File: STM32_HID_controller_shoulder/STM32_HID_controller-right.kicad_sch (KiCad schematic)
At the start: 5 parts, among them J4 Conn_01x03_Socket

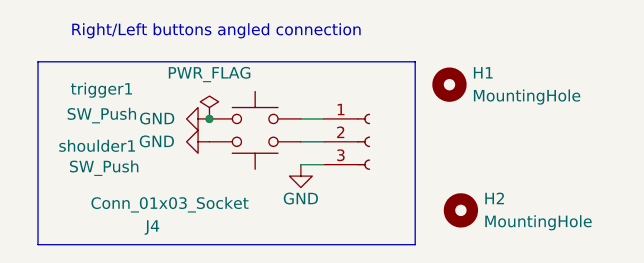
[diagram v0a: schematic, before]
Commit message: changed shoulder to right orientation
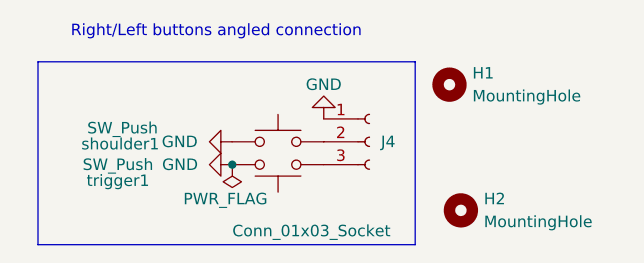
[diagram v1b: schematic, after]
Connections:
- net GND: now also J4.1 (Pin_1); no longer J4.3 (Pin_3)
- net at trigger1.2: now also J4.3 (Pin_3); no longer J4.1 (Pin_1)
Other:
- moved on the sheet: shoulder1, trigger1
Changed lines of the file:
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@@
 	)
 	(junction
-		(at 76.2 62.23)
+		(at 78.74 67.31)
 		(diameter 0)
 		(color 0 0 0 0)
 	)
-	(wire
-		(pts
-			(xy 86.36 62.23) (xy 88.9 62.23)
-		)
-		(stroke
-			(width 0)
-			(type default)
-		)
-	)
-	(wire
-		(pts
-			(xy 86.36 67.31) (xy 88.9 67.31)
-		)
-		(stroke
-			(width 0)
-			(type default)
-		)
-	)
-	(wire
-		(pts
-			(xy 86.36 64.77) (xy 88.9 64.77)
-		)
-		(stroke
-			(width 0)
-			(type default)
-		)
-	)
 	(symbol
 		(lib_id "power:GND")
-		(at 76.2 64.77 270)
+		(at 78.74 64.77 270)
 		(unit 1)
 		(exclude_from_sim no)
@@
 		(dnp no)
 		(property "Reference" "#PWR054"
-			(at 69.85 64.77 0)
+			(at 72.39 64.77 0)
 			(effects
 				(font
@@
 		)
 		(property "Value" "GND"
-			(at 70.358 64.77 90)
+			(at 72.898 64.77 90)
 			(effects
 				(font
@@
 		)
 		(property "Footprint" ""
-			(at 76.2 64.77 0)
+			(at 78.74 64.77 0)
 			(effects
 				(font
@@
 		)
 		(property "Datasheet" ""
-			(at 76.2 64.77 0)
+			(at 78.74 64.77 0)
 			(effects
 				(font
@@
 		)
 		(property "Description" "Power symbol creates a global label with name \"GND\" , ground"
-			(at 76.2 64.77 0)
+			(at 78.74 64.77 0)
 			(effects
 				(font
@@
 	(symbol
 		(lib_id "Switch:SW_Push")
-		(at 81.28 64.77 180)
+		(at 83.82 64.77 0)
+		(mirror y)
 		(unit 1)
 		(exclude_from_sim no)
@@
 		(dnp no)
 		(property "Reference" "shoulder1"
-			(at 63.754 65.278 0)
+			(at 66.294 65.024 0)
 			(effects
 				(font
@@
 		)
 		(property "Value" "SW_Push"
-			(at 64.516 67.564 0)
+			(at 66.548 63.246 0)
 			(effects
 				(font
@@
 		)
 		(property "Footprint" "Button_Switch_THT:SW_PUSH-12mm_Wuerth-430476085716"
-			(at 81.28 69.85 0)
+			(at 83.82 59.69 0)
 			(effects
 				(font
@@
 		)
 		(property "Datasheet" "~"
-			(at 81.28 69.85 0)
+			(at 83.82 59.69 0)
 			(effects
 				(font
@@
 		)
 		(property "Description" "Push button switch, generic, two pins"
-			(at 81.28 64.77 0)
+			(at 83.82 64.77 0)
 			(effects
 				(font
@@
 	(symbol
 		(lib_id "power:GND")
-		(at 86.36 67.31 0)
+		(at 88.9 62.23 180)
 		(unit 1)
 		(exclude_from_sim no)
@@
 		(dnp no)
 		(property "Reference" "#PWR053"
-			(at 86.36 73.66 0)
+			(at 88.9 55.88 0)
 			(effects
 				(font
@@
 		)
 		(property "Value" "GND"
-			(at 86.36 71.12 0)
+			(at 88.9 58.42 0)
 			(effects
 				(font
@@
 		)
 		(property "Footprint" ""
-			(at 86.36 67.31 0)
+			(at 88.9 62.23 0)
 			(effects
 				(font
@@
 		)
 		(property "Datasheet" ""
-			(at 86.36 67.31 0)
+			(at 88.9 62.23 0)
 			(effects
 				(font
@@
 		)
 		(property "Description" "Power symbol creates a global label with name \"GND\" , ground"
-			(at 86.36 67.31 0)
+			(at 88.9 62.23 0)
 			(effects
 				(font
@@
 	(symbol
 		(lib_id "Switch:SW_Push")
-		(at 81.28 62.23 0)
+		(at 83.82 67.31 0)
+		(mirror x)
 		(unit 1)
 		(exclude_from_sim no)
@@
 		(dnp no)
 		(property "Reference" "trigger1"
-			(at 64.262 58.928 0)
+			(at 66.04 69.088 0)
 			(effects
 				(font
@@
 		)
 		(property "Value" "SW_Push"
-			(at 64.262 61.722 0)
+			(at 66.04 67.31 0)
 			(effects
 				(font
@@
 		)
 		(property "Footprint" "Button_Switch_THT:SW_DIP_SPSTx01_Piano_10.8x4.1mm_W7.62mm_P2.54mm"
-			(at 81.28 57.15 0)
+			(at 83.82 72.39 0)
 			(effects
 				(font
@@
 		)
 		(property "Datasheet" "~"
-			(at 81.28 57.15 0)
+			(at 83.82 72.39 0)
 			(effects
 				(font
@@
 		)
 		(property "Description" "Push button switch, generic, two pins"
-			(at 81.28 62.23 0)
+			(at 83.82 67.31 0)
 			(effects
 				(font
@@
 	(symbol
 		(lib_id "power:GND")
-		(at 76.2 62.23 270)
+		(at 78.74 67.31 270)
 		(unit 1)
 		(exclude_from_sim no)
@@
 		(fields_autoplaced yes)
 		(property "Reference" "#PWR018"
-			(at 69.85 62.23 0)
+			(at 72.39 67.31 0)
 			(effects
 				(font
@@
 		)
 		(property "Value" "GND"
-			(at 72.39 62.2299 90)
+			(at 74.93 67.3099 90)
 			(effects
 				(font
@@
 		)
 		(property "Footprint" ""
-			(at 76.2 62.23 0)
+			(at 78.74 67.31 0)
 			(effects
 				(font
@@
 		)
 		(property "Datasheet" ""
-			(at 76.2 62.23 0)
+			(at 78.74 67.31 0)
 			(effects
 				(font
@@
 		)
 		(property "Description" "Power symbol creates a global label with name \"GND\" , ground"
-			(at 76.2 62.23 0)
+			(at 78.74 67.31 0)
 			(effects
 				(font
@@
 	(symbol
 		(lib_id "power:PWR_FLAG")
-		(at 76.2 62.23 0)
-		(unit 1)
-		(exclude_from_sim no)
-		(in_bom yes)
-		(on_board yes)
-		(dnp no)
-		(fields_autoplaced yes)
+		(at 78.74 67.31 0)
+		(mirror x)
+		(unit 1)
+		(exclude_from_sim no)
+		(in_bom yes)
+		(on_board yes)
+		(dnp no)
 		(property "Reference" "#FLG01"
-			(at 76.2 60.325 0)
+			(at 78.74 69.215 0)
 			(effects
 				(font
@@
 		)
 		(property "Value" "PWR_FLAG"
-			(at 76.2 57.15 0)
+			(at 77.978 71.12 0)
 			(effects
 				(font
@@
 		)
 		(property "Footprint" ""
-			(at 76.2 62.23 0)
+			(at 78.74 67.31 0)
 			(effects
 				(font
@@
 		)
 		(property "Datasheet" "~"
-			(at 76.2 62.23 0)
+			(at 78.74 67.31 0)
 			(effects
 				(font
@@
 		)
 		(property "Description" "Special symbol for telling ERC where power comes from"
-			(at 76.2 62.23 0)
+			(at 78.74 67.31 0)
 			(effects
 				(font
@@
 		(dnp no)
 		(property "Reference" "J4"
-			(at 69.088 74.168 0)
+			(at 95.25 64.77 0)
 			(effects
 				(font
@@
 		)
 		(property "Value" "Conn_01x03_Socket"
-			(at 62.992 71.628 0)
-			(effects
-				(font
+			(at 78.74 74.676 0)
+			(effects
+				(font
